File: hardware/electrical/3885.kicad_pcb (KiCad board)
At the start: 4 copper layers, 33 x 77 mm, 109 parts, among them J1 USB_B_Micro, J2 TC2030, J3 Micro_SD_Card_Det1, J4 JST-PH, J5 FFC, Q1 AO3400A, Q2 AO3400A, Q3 AO3401A, Q4 AO3401A, Q5 2N7002, Q6 AO3401A, Q7 AO3401A, Q8 2N7002, SW1 TS-1187A-B-A-B, SW2 EVQP7C01K, U1 USB3300-EZK, U2 TP4054, U3 TLV70028DCKR, U4 WL2803E33-5/TR, U5 AP9101CK6-AYTRG1, U6 APX803S-31SA-7, U8 STM32F446VET6, U9 TLV70012DCKR, X2 SG-8018CA 24.0000M-TJHPA3r, Y1 24MHz, Y2 32.768kHz

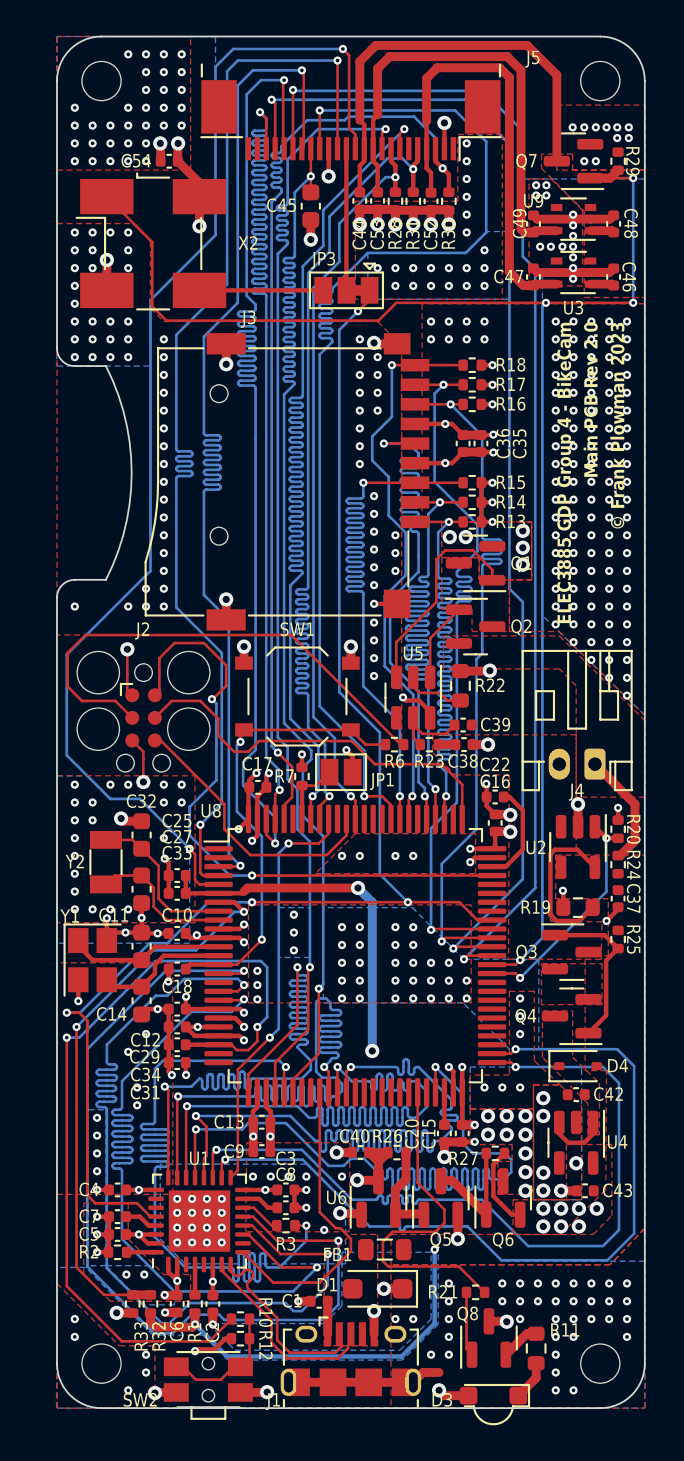
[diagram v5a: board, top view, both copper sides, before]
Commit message: Fix silkscreen DRC errors
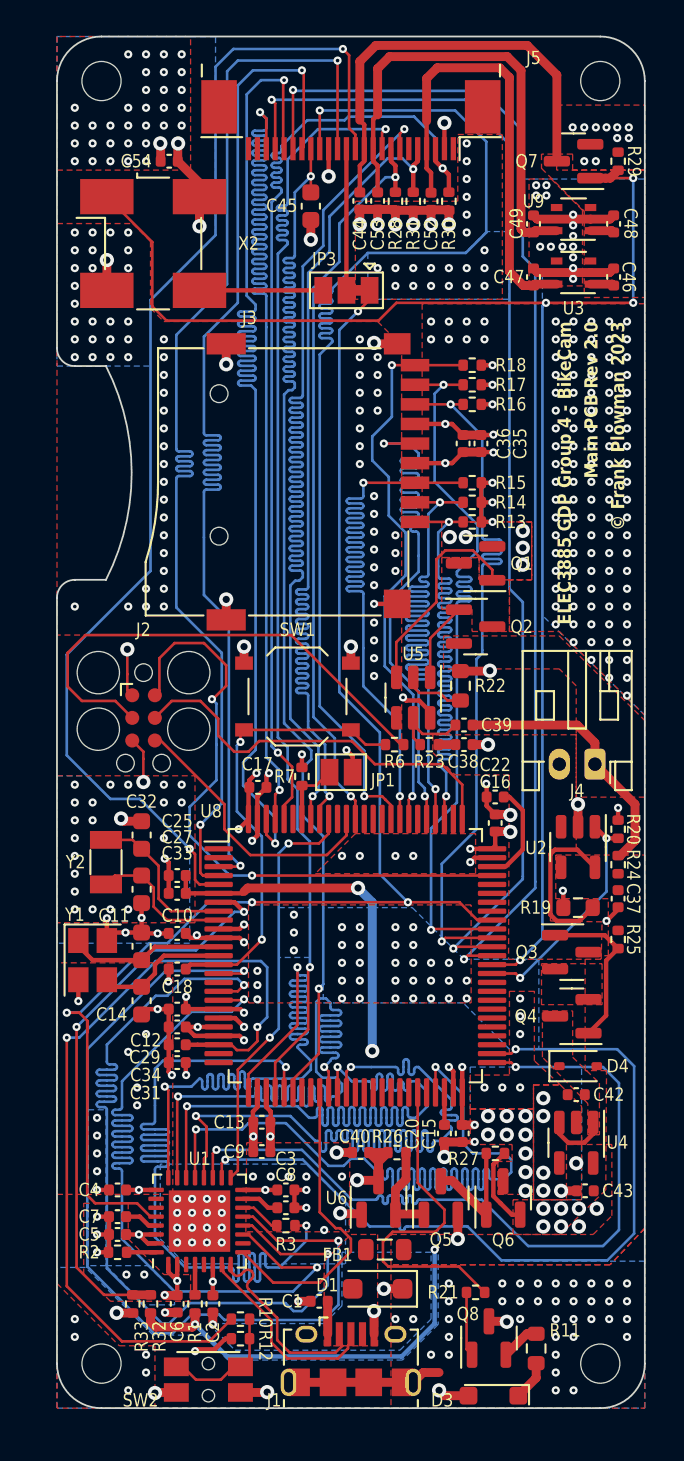
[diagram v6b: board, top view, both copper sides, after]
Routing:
- net -BATT: track 6.53 -> 15.0 mm
